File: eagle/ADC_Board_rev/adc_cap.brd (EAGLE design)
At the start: 98.7 x 73.7 mm, 58 parts, among them Q1 BSS84, Q2 BSS84, Q3 BSS84, Q4 BSS84, Q5 BSS84, Q6 BSS84, Q7 BSS84, Q8 BSS84

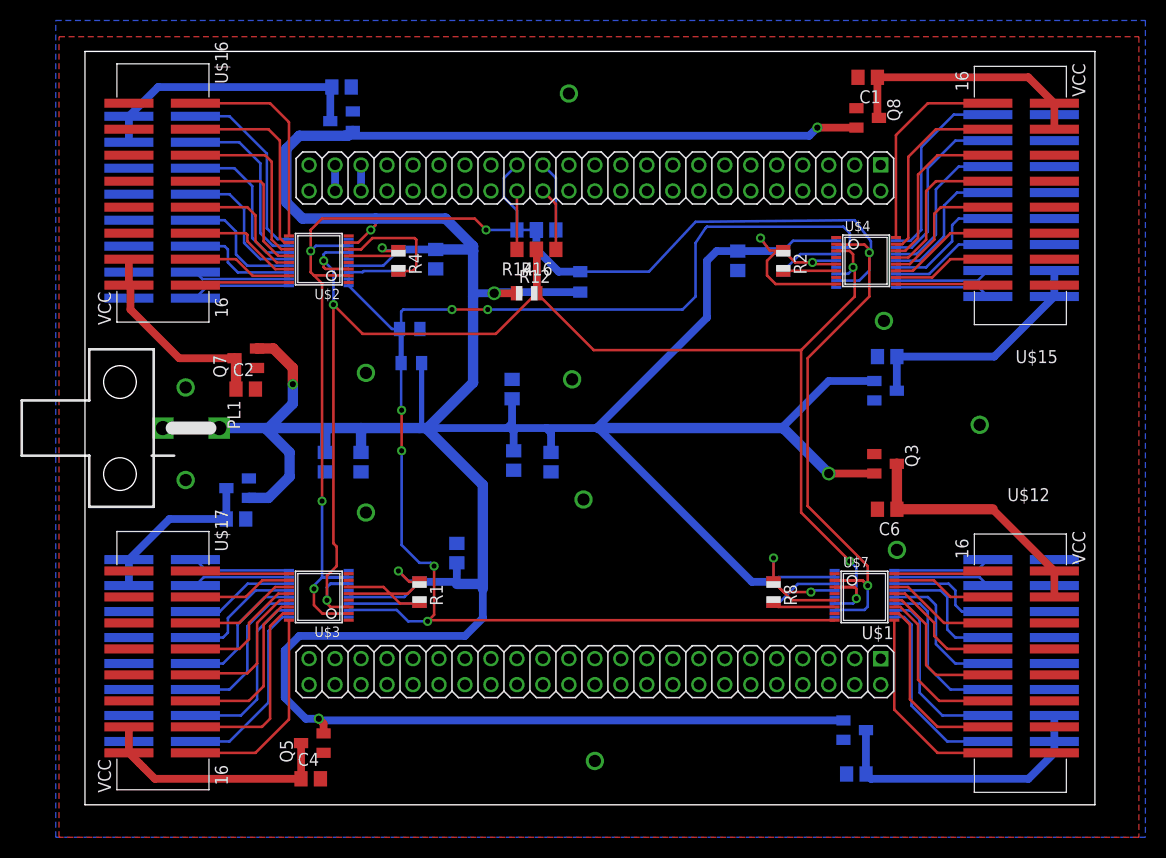
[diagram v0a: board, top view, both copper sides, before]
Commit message: update to adc cape
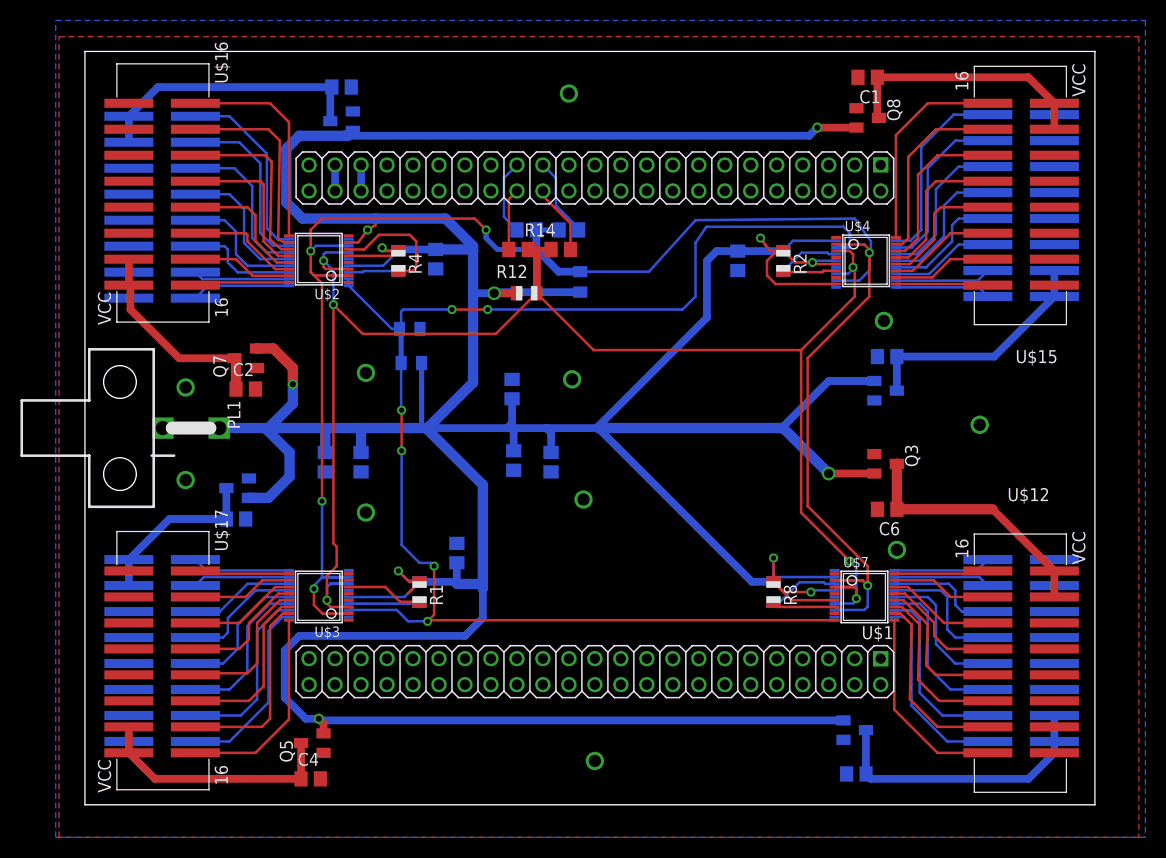
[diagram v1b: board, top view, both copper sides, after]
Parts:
- moved R15 2.22 mm to (47.3, 56.2)
- moved R16 1.43 mm to (46.5, 54.3)
- moved R14 0.79 mm to (42.4, 54.3)
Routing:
- net VCC: track 499.2 -> 493.8 mm
- net N$84: track 176.2 -> 179.9 mm
- net N$55: track 153.0 -> 155.2 mm
- net N$81: track 6.88 -> 7.80 mm
- net N$86: track 6.24 -> 6.83 mm
